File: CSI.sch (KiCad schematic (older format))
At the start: 19 parts

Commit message: update power mark,
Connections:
- net labels added: VCC-IO
- net labels removed: Vcc-io
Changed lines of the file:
@@
 $Descr A4 11693 8268
 encoding utf-8
-Sheet 10 33
+Sheet 10 34
 Title ""
 Date ""
@@
 $EndComp
 $Comp
-L taobao-components:Vcc-io #PWR?
-U 1 1 5C25BF2D
-P 8150 5450
-AR Path="/5C259FA6/5C25BF2D" Ref="#PWR?"  Part="1"
-AR Path="/5C21B42E/5C25BF2D" Ref="#PWR?"  Part="1"
-F 0 "#PWR?" H 8150 5300 50  0001 C CNN
-F 1 "Vcc-io" H 8155 5573 50  0000 C CNN
-F 2 "" H 8150 5450 50  0001 C CNN
-F 3 "" H 8150 5450 50  0001 C CNN
-	1    8150 5450
-	1    0    0    -1
-$EndComp
-$Comp
 L taobao-r:R513,0603 R?
 U 1 1 5C25BF91
@@
 $EndComp
 $Comp
-L taobao-components:Vcc-io #PWR?
-U 1 1 5C2627FF
-P 8150 4400
-AR Path="/5C259FA6/5C2627FF" Ref="#PWR?"  Part="1"
-AR Path="/5C21B42E/5C2627FF" Ref="#PWR?"  Part="1"
-F 0 "#PWR?" H 8150 4250 50  0001 C CNN
-F 1 "Vcc-io" H 8155 4523 50  0000 C CNN
-F 2 "" H 8150 4400 50  0001 C CNN
-F 3 "" H 8150 4400 50  0001 C CNN
-	1    8150 4400
-	1    0    0    -1
-$EndComp
-$Comp
 L taobao-r:R513,0603 R?
 U 1 1 5C262805
@@
 $EndComp
 $Comp
-L taobao-components:Vcc-io #PWR?
-U 1 1 5C266FD7
-P 7650 2850
-AR Path="/5C259FA6/5C266FD7" Ref="#PWR?"  Part="1"
-AR Path="/5C21B42E/5C266FD7" Ref="#PWR?"  Part="1"
-F 0 "#PWR?" H 7650 2700 50  0001 C CNN
-F 1 "Vcc-io" H 7655 2973 50  0000 C CNN
-F 2 "" H 7650 2850 50  0001 C CNN
-F 3 "" H 7650 2850 50  0001 C CNN
-	1    7650 2850
-	1    0    0    -1
-$EndComp
-$Comp
 L taobao-c:C475,0603 C?
 U 1 1 5C266FE3
@@
 $EndComp
 $Comp
-L taobao-components:Vcc-io #PWR?
-U 1 1 5C276840
-P 5400 3050
-AR Path="/5C259FA6/5C276840" Ref="#PWR?"  Part="1"
-AR Path="/5C21B42E/5C276840" Ref="#PWR?"  Part="1"
-F 0 "#PWR?" H 5400 2900 50  0001 C CNN
-F 1 "Vcc-io" V 5405 3128 50  0000 L CNN
-F 2 "" H 5400 3050 50  0001 C CNN
-F 3 "" H 5400 3050 50  0001 C CNN
-	1    5400 3050
-	0    -1   -1   0
-$EndComp
-$Comp
 L taobao-r:R0,0603 R?
 U 1 1 5C276A4E
@@
 Wire Wire Line
 	1650 3650 2300 3650
+$Comp
+L taobao-components:VCC-IO #PWR?
+U 1 1 5C7D814D
+P 7650 2850
+F 0 "#PWR?" H 7650 2700 50  0001 C CNN
+F 1 "VCC-IO" H 7700 3000 50  0000 C CNN
+F 2 "" H 7650 2850 50  0001 C CNN
+F 3 "" H 7650 2850 50  0001 C CNN
+	1    7650 2850
+	1    0    0    -1
+$EndComp
+$Comp
+L taobao-components:VCC-IO #PWR?
+U 1 1 5C7D837C
+P 8150 5450
+F 0 "#PWR?" H 8150 5300 50  0001 C CNN
+F 1 "VCC-IO" H 8200 5600 50  0000 C CNN
+F 2 "" H 8150 5450 50  0001 C CNN
+F 3 "" H 8150 5450 50  0001 C CNN
+	1    8150 5450
+	1    0    0    -1
+$EndComp
+$Comp
+L taobao-components:VCC-IO #PWR?
+U 1 1 5C7D85D2
+P 8150 4400
+F 0 "#PWR?" H 8150 4250 50  0001 C CNN
+F 1 "VCC-IO" H 8200 4550 50  0000 C CNN
+F 2 "" H 8150 4400 50  0001 C CNN
+F 3 "" H 8150 4400 50  0001 C CNN
+	1    8150 4400
+	1    0    0    -1
+$EndComp
+$Comp
+L taobao-components:VCC-IO #PWR?
+U 1 1 5C7D8654
+P 5400 3050
+F 0 "#PWR?" H 5400 2900 50  0001 C CNN
+F 1 "VCC-IO" V 5450 3150 50  0000 L CNN
+F 2 "" H 5400 3050 50  0001 C CNN
+F 3 "" H 5400 3050 50  0001 C CNN
+	1    5400 3050
+	0    -1   -1   0
+$EndComp
 $EndSCHEMATC

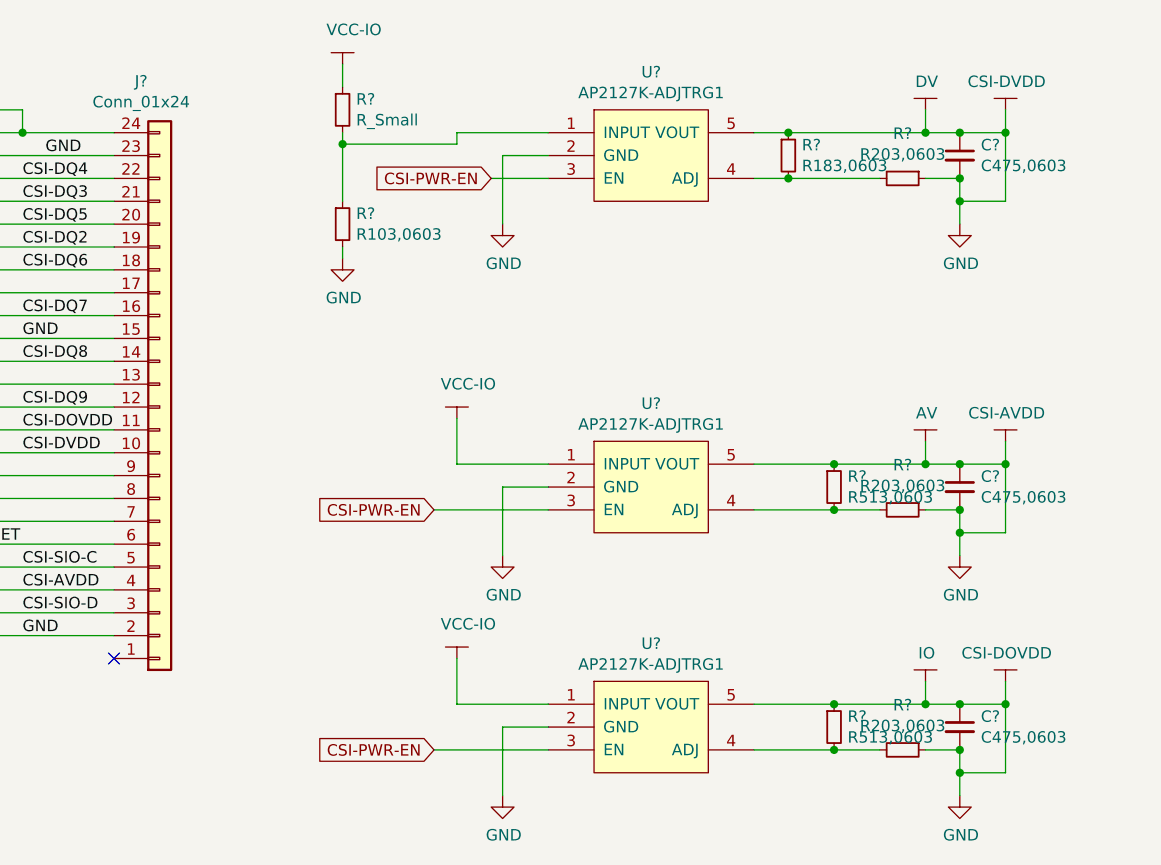
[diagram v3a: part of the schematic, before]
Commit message: update HDMI,
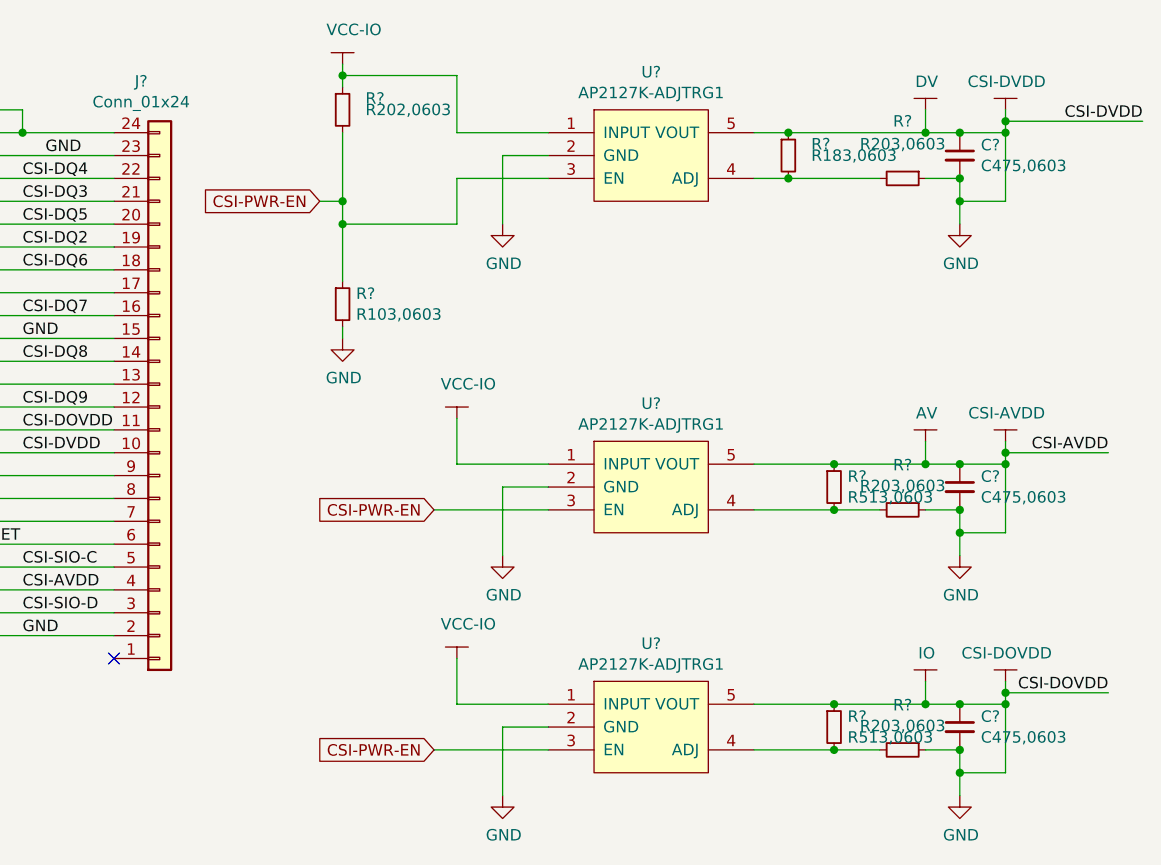
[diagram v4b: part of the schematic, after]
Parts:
- removed R?: R_Small, symbol Device:R_Small
- added R?: R202,0603, Resistor_SMD:R_0603_1608Metric_Pad1.05x0.95mm_HandSolder, symbol taobao-r:R202,0603
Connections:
- wire segments 112 -> 123
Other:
- moved on the sheet: R?
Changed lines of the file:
@@
 $Descr A4 11693 8268
 encoding utf-8
-Sheet 10 33
+Sheet 9 33
 Title ""
 Date ""
@@
 Connection ~ 10550 5650
 Wire Wire Line
-	10550 5650 10550 5550
+	10550 5650 10550 5600
 $Comp
 L taobao-components:AP2127K-ADJTRG1 U?
@@
 Connection ~ 10550 4600
 Wire Wire Line
-	10550 4600 10550 4500
+	10550 4600 10550 4550
 $Comp
 L taobao-components:CSI-AVDD #PWR?
@@
 AR Path="/5C259FA6/5C266FE9" Ref="R?"  Part="1"
 AR Path="/5C21B42E/5C266FE9" Ref="R?"  Part="1"
-F 0 "R?" V 9904 3350 50  0000 C CNN
-F 1 "R203,0603" V 9995 3350 50  0000 C CNN
+F 0 "R?" V 9850 3350 50  0000 C CNN
+F 1 "R203,0603" V 9950 3350 50  0000 C CNN
 F 2 "Resistor_SMD:R_0603_1608Metric_Pad1.05x0.95mm_HandSolder" H 10100 3350 50  0001 C CNN
 F 3 "~" H 10100 3350 50  0001 C CNN
@@
 	1    0    0    -1
 $EndComp
-Text GLabel 8300 3350 0    50   Input ~ 0
+Text GLabel 7550 3450 0    50   Input ~ 0
 CSI-PWR-EN
 Wire Wire Line
@@
 Wire Wire Line
 	8150 3150 8550 3150
-Wire Wire Line
-	8550 3350 8300 3350
 $Comp
 L power:GND #PWR?
@@
 Connection ~ 10550 3150
 Wire Wire Line
-	10550 3150 10550 3050
-$Comp
-L Device:R_Small R?
-U 1 1 5C268BFC
-P 7650 3050
-AR Path="/5C259FA6/5C268BFC" Ref="R?"  Part="1"
-AR Path="/5C21B42E/5C268BFC" Ref="R?"  Part="1"
-F 0 "R?" H 7709 3096 50  0000 L CNN
-F 1 "R_Small" H 7709 3005 50  0000 L CNN
-F 2 "" H 7650 3050 50  0001 C CNN
-F 3 "~" H 7650 3050 50  0001 C CNN
-	1    7650 3050
-	1    0    0    -1
-$EndComp
+	10550 3150 10550 3100
 $Comp
 L taobao-r:R103,0603 R?
 U 1 1 5C268E1A
-P 7650 3550
+P 7650 3900
 AR Path="/5C259FA6/5C268E1A" Ref="R?"  Part="1"
 AR Path="/5C21B42E/5C268E1A" Ref="R?"  Part="1"
-F 0 "R?" H 7709 3596 50  0000 L CNN
-F 1 "R103,0603" H 7709 3505 50  0000 L CNN
-F 2 "Resistor_SMD:R_0603_1608Metric_Pad1.05x0.95mm_HandSolder" H 7650 3550 50  0001 C CNN
-F 3 "~" H 7650 3550 50  0001 C CNN
-	1    7650 3550
+F 0 "R?" H 7709 3946 50  0000 L CNN
+F 1 "R103,0603" H 7709 3855 50  0000 L CNN
+F 2 "Resistor_SMD:R_0603_1608Metric_Pad1.05x0.95mm_HandSolder" H 7650 3900 50  0001 C CNN
+F 3 "~" H 7650 3900 50  0001 C CNN
+	1    7650 3900
 	1    0    0    -1
 $EndComp
@@
 L power:GND #PWR?
 U 1 1 5C268E5A
-P 7650 3700
+P 7650 4050
 AR Path="/5C259FA6/5C268E5A" Ref="#PWR?"  Part="1"
 AR Path="/5C21B42E/5C268E5A" Ref="#PWR?"  Part="1"
-F 0 "#PWR?" H 7650 3450 50  0001 C CNN
-F 1 "GND" H 7655 3527 50  0000 C CNN
-F 2 "" H 7650 3700 50  0001 C CNN
-F 3 "" H 7650 3700 50  0001 C CNN
-	1    7650 3700
+F 0 "#PWR?" H 7650 3800 50  0001 C CNN
+F 1 "GND" H 7655 3877 50  0000 C CNN
+F 2 "" H 7650 4050 50  0001 C CNN
+F 3 "" H 7650 4050 50  0001 C CNN
+	1    7650 4050
 	1    0    0    -1
 $EndComp
 Wire Wire Line
-	7650 3650 7650 3700
-Wire Wire Line
-	7650 2850 7650 2950
-Wire Wire Line
-	7650 3150 7650 3200
+	7650 4000 7650 4050
 Wire Wire Line
-	7650 3200 8150 3200
-Wire Wire Line
-	8150 3200 8150 3150
-Connection ~ 7650 3200
-Wire Wire Line
-	7650 3200 7650 3450
+	7650 2850 7650 2900
 Wire Wire Line
 	9450 3150 9600 3150
@@
 AR Path="/5C259FA6/5C26E97D" Ref="R?"  Part="1"
 AR Path="/5C21B42E/5C26E97D" Ref="R?"  Part="1"
-F 0 "R?" H 9659 3296 50  0000 L CNN
-F 1 "R183,0603" H 9659 3205 50  0000 L CNN
+F 0 "R?" H 9700 3300 50  0000 L CNN
+F 1 "R183,0603" H 9700 3250 50  0000 L CNN
 F 2 "Resistor_SMD:R_0603_1608Metric_Pad1.05x0.95mm_HandSolder" H 9600 3250 50  0001 C CNN
 F 3 "~" H 9600 3250 50  0001 C CNN
@@
 	0    -1   -1   0
 $EndComp
+$Comp
+L taobao-r:R202,0603 R?
+U 1 1 5C49AD94
+P 7650 3050
+F 0 "R?" H 7750 3100 50  0000 L CNN
+F 1 "R202,0603" H 7750 3050 50  0000 L CNN
+F 2 "Resistor_SMD:R_0603_1608Metric_Pad1.05x0.95mm_HandSolder" H 7650 3050 50  0001 C CNN
+F 3 "~" H 7650 3050 50  0001 C CNN
+	1    7650 3050
+	1    0    0    -1
+$EndComp
+Wire Wire Line
+	7650 2900 8150 2900
+Wire Wire Line
+	8150 2900 8150 3150
+Connection ~ 7650 2900
+Wire Wire Line
+	7650 2900 7650 2950
+Wire Wire Line
+	7650 3150 7650 3450
+Wire Wire Line
+	7550 3450 7650 3450
+Connection ~ 7650 3450
+Wire Wire Line
+	7650 3450 7650 3550
+Wire Wire Line
+	8150 3350 8150 3550
+Wire Wire Line
+	8150 3550 7650 3550
+Wire Wire Line
+	8150 3350 8550 3350
+Connection ~ 7650 3550
+Wire Wire Line
+	7650 3550 7650 3800
+Text Label 11150 3100 2    50   ~ 0
+CSI-DVDD
+Wire Wire Line
+	11150 3100 10550 3100
+Connection ~ 10550 3100
+Wire Wire Line
+	10550 3100 10550 3050
+Text Label 11000 4550 2    50   ~ 0
+CSI-AVDD
+Wire Wire Line
+	11000 4550 10550 4550
+Connection ~ 10550 4550
+Wire Wire Line
+	10550 4550 10550 4500
+Text Label 11000 5600 2    50   ~ 0
+CSI-DOVDD
+Wire Wire Line
+	11000 5600 10550 5600
+Connection ~ 10550 5600
+Wire Wire Line
+	10550 5600 10550 5550
 $EndSCHEMATC

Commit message: update,
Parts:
- added C? (x2): C_NC,0603, Capacitor_SMD:C_0603_1608Metric_Pad1.05x0.95mm_HandSolder, symbol taobao-components:C_NC,0603
- added R? (x2): R202,0603, Resistor_SMD:R_0603_1608Metric_Pad1.05x0.95mm_HandSolder, symbol taobao-r:R202,0603
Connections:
- net labels added: CSI0-RESET#, CSI0-RST#
- net labels removed: CSI0-D18RESET, CSI0-RESET, CSI0-RST
- wire segments 123 -> 131
